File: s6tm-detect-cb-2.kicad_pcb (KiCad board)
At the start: 4 copper layers, 90 x 50 mm, 173 parts, among them J1 Conn_Coaxial, J2 Conn_01x04_Pin, J3 USB_C_Receptacle_USB2.0_14P, J4 Conn_01x04, J5 Conn_01x04, J6 USB_C_Receptacle_USB2.0_14P, J7 Conn_01x04_Pin, J8 SIM_Card_Shielded, J9 Conn_Coaxial, Q1 AO3400A, Q2 MMBT3904, Q3 MMBT3904, Q4 MMBT3904, SW1 SW_Push, SW2 SW_Push, SW3 SW_Push, SW4 SW_Push, U1 W25Q128JVS, U10 TPS6282x, U11 TPS6282x, U12 TPS259472A, U13 TPD3F303DPV, U14 SIM7080G, U15 SN74LV1T125DBV, U16 SN74LV1T125DBV, U17 SN74LV1T125DBV, U18 SN74LV1T125DBV, U19 SN74LV1T125DBV, U2 SN65HVD230, U3 PCF85263ATL, U4 MS5607, U5 ESP32-S3FH4R2, U6 HTU21, U8 VL53L0CXV0DH1, U9 NextPM, Y1 32k768, Y2 48M

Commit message: pcb: route spi flash
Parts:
- moved R8 0.50 mm to (138.5, 85.5)
- moved R9 0.50 mm to (139.5, 85.5)
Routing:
- net /FLASH_CS: track 0.00 -> 19.9 mm
- net /FLASH_IO1: track 0.00 -> 15.8 mm
- net /FLASH_IO0: track 0.00 -> 9.59 mm
- net /FLASH_CLK: track 0.00 -> 5.24 mm
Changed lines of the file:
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@@
 	(footprint "Resistor_SMD:R_0402_1005Metric"
 		(layer "F.Cu")
-		(at 139 85.49 -90)
+		(at 138.5 85.49 -90)
 		(descr "Resistor SMD 0402 (1005 Metric), square (rectangular) end terminal, IPC-7351 nominal, (Body size source: IPC-SM-782 page 72, https://www.pcb-3d.com/wordpress/wp-content/uploads/ipc-sm-782a_amendment_1_and_2.pdf)")
 		(tags "resistor")
@@
 	(footprint "Resistor_SMD:R_0402_1005Metric"
 		(layer "F.Cu")
-		(at 140 85.49 -90)
+		(at 139.5 85.49 -90)
 		(descr "Resistor SMD 0402 (1005 Metric), square (rectangular) end terminal, IPC-7351 nominal, (Body size source: IPC-SM-782 page 72, https://www.pcb-3d.com/wordpress/wp-content/uploads/ipc-sm-782a_amendment_1_and_2.pdf)")
 		(tags "resistor")
@@
 	)
 	(segment
+		(start 146.25 88.25)
+		(end 147.25 87.25)
+		(width 0.2)
+		(layer "F.Cu")
+		(net "/FLASH_CS")
+	)
+	(segment
+		(start 146.9125 77.9125)
+		(end 144.905 77.9125)
+		(width 0.2)
+		(layer "F.Cu")
+		(net "/FLASH_CS")
+	)
+	(segment
+		(start 143.1 88.9)
+		(end 143.75 88.25)
+		(width 0.2)
+		(layer "F.Cu")
+		(net "/FLASH_CS")
+	)
+	(segment
+		(start 143.75 88.25)
+		(end 146.25 88.25)
+		(width 0.2)
+		(layer "F.Cu")
+		(net "/FLASH_CS")
+	)
+	(segment
+		(start 147.25 87.25)
+		(end 147.25 78.25)
+		(width 0.2)
+		(layer "F.Cu")
+		(net "/FLASH_CS")
+	)
+	(segment
+		(start 143.1 90.3)
+		(end 143.1 88.9)
+		(width 0.2)
+		(layer "F.Cu")
+		(net "/FLASH_CS")
+	)
+	(segment
+		(start 144.905 77.9125)
+		(end 144.905 75.895)
+		(width 0.2)
+		(layer "F.Cu")
+		(net "/FLASH_CS")
+	)
+	(segment
+		(start 144.905 75.895)
+		(end 144.76 75.75)
+		(width 0.2)
+		(layer "F.Cu")
+		(net "/FLASH_CS")
+	)
+	(segment
+		(start 147.25 78.25)
+		(end 146.9125 77.9125)
+		(width 0.2)
+		(layer "F.Cu")
+		(net "/FLASH_CS")
+	)
+	(segment
+		(start 141.25 86.5)
+		(end 140.75 86.5)
+		(width 0.2)
+		(layer "F.Cu")
+		(net "/FLASH_IO1")
+	)
+	(segment
+		(start 143.635 80.365)
+		(end 143.635 77.9125)
+		(width 0.2)
+		(layer "F.Cu")
+		(net "/FLASH_IO1")
+	)
+	(segment
+		(start 140.25 82)
+		(end 141 81.25)
+		(width 0.2)
+		(layer "F.Cu")
+		(net "/FLASH_IO1")
+	)
+	(segment
+		(start 141 81.25)
+		(end 142.75 81.25)
+		(width 0.2)
+		(layer "F.Cu")
+		(net "/FLASH_IO1")
+	)
+	(segment
+		(start 142.75 81.25)
+		(end 143.635 80.365)
+		(width 0.2)
+		(layer "F.Cu")
+		(net "/FLASH_IO1")
+	)
+	(segment
+		(start 140.75 86.5)
+		(end 140.25 86)
+		(width 0.2)
+		(layer "F.Cu")
+		(net "/FLASH_IO1")
+	)
+	(segment
+		(start 141.9 90.3)
+		(end 141.9 87.15)
+		(width 0.2)
+		(layer "F.Cu")
+		(net "/FLASH_IO1")
+	)
+	(segment
+		(start 140.25 86)
+		(end 140.25 82)
+		(width 0.2)
+		(layer "F.Cu")
+		(net "/FLASH_IO1")
+	)
+	(segment
+		(start 141.9 87.15)
+		(end 141.25 86.5)
+		(width 0.2)
+		(layer "F.Cu")
+		(net "/FLASH_IO1")
+	)
+	(segment
+		(start 143 84)
+		(end 142.75 83.75)
+		(width 0.2)
+		(layer "F.Cu")
+		(net "/FLASH_IO0")
+	)
+	(segment
+		(start 141.405 83.75)
+		(end 141.095 84.06)
+		(width 0.2)
+		(layer "F.Cu")
+		(net "/FLASH_IO0")
+	)
+	(segment
+		(start 142.75 83.75)
+		(end 141.405 83.75)
+		(width 0.2)
+		(layer "F.Cu")
+		(net "/FLASH_IO0")
+	)
+	(segment
+		(start 141.095 84.06)
+		(end 141.095 85.0875)
+		(width 0.2)
+		(layer "F.Cu")
+		(net "/FLASH_IO0")
+	)
+	(segment
+		(start 142.7 90.3)
+		(end 142.7 86.3)
+		(width 0.2)
+		(layer "F.Cu")
+		(net "/FLASH_IO0")
+	)
+	(segment
+		(start 142.7 86.3)
+		(end 143 86)
+		(width 0.2)
+		(layer "F.Cu")
+		(net "/FLASH_IO0")
+	)
+	(segment
+		(start 143 86)
+		(end 143 84)
+		(width 0.2)
+		(layer "F.Cu")
+		(net "/FLASH_IO0")
+	)
+	(segment
+		(start 142.3 85.1525)
+		(end 142.365 85.0875)
+		(width 0.2)
+		(layer "F.Cu")
+		(net "/FLASH_CLK")
+	)
+	(segment
+		(start 142.3 90.3)
+		(end 142.3 85.1525)
+		(width 0.2)
+		(layer "F.Cu")
+		(net "/FLASH_CLK")
+	)
+	(segment

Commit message: pcb: route can
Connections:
- U5 pad 13: /CAN_RX -> /CAN_TX
- U5 pad 14: /CAN_TX -> /CAN_RX
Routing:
- net CANL: track 0.00 -> 40.5 mm
- net /CAN_RX: track 0.00 -> 35.8 mm
- net /CAN_TX: track 0.00 -> 31.6 mm
- net CANH: track 0.00 -> 30.0 mm
- net Net-(JP1-B): track 0.00 -> 2.89 mm
- net GND: vias 188 -> 192

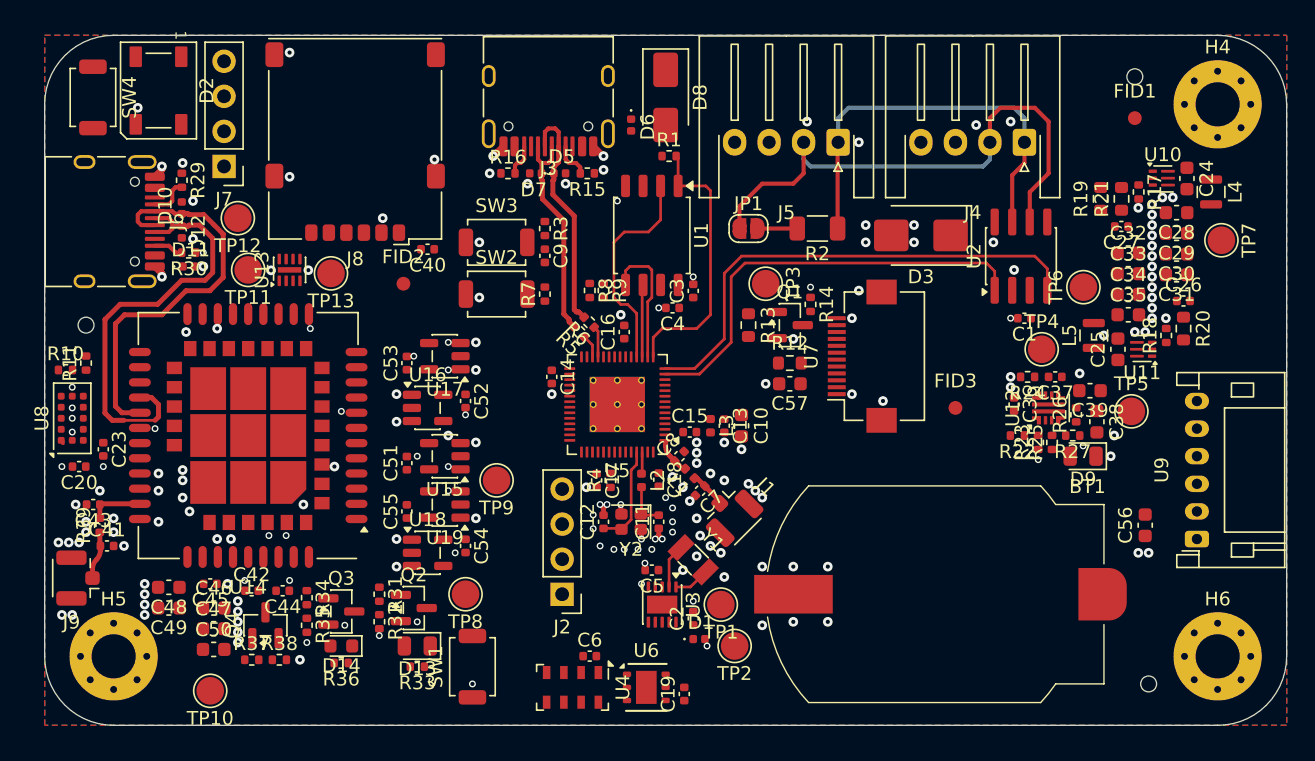
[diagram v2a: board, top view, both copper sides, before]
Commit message: pcb: route uarts
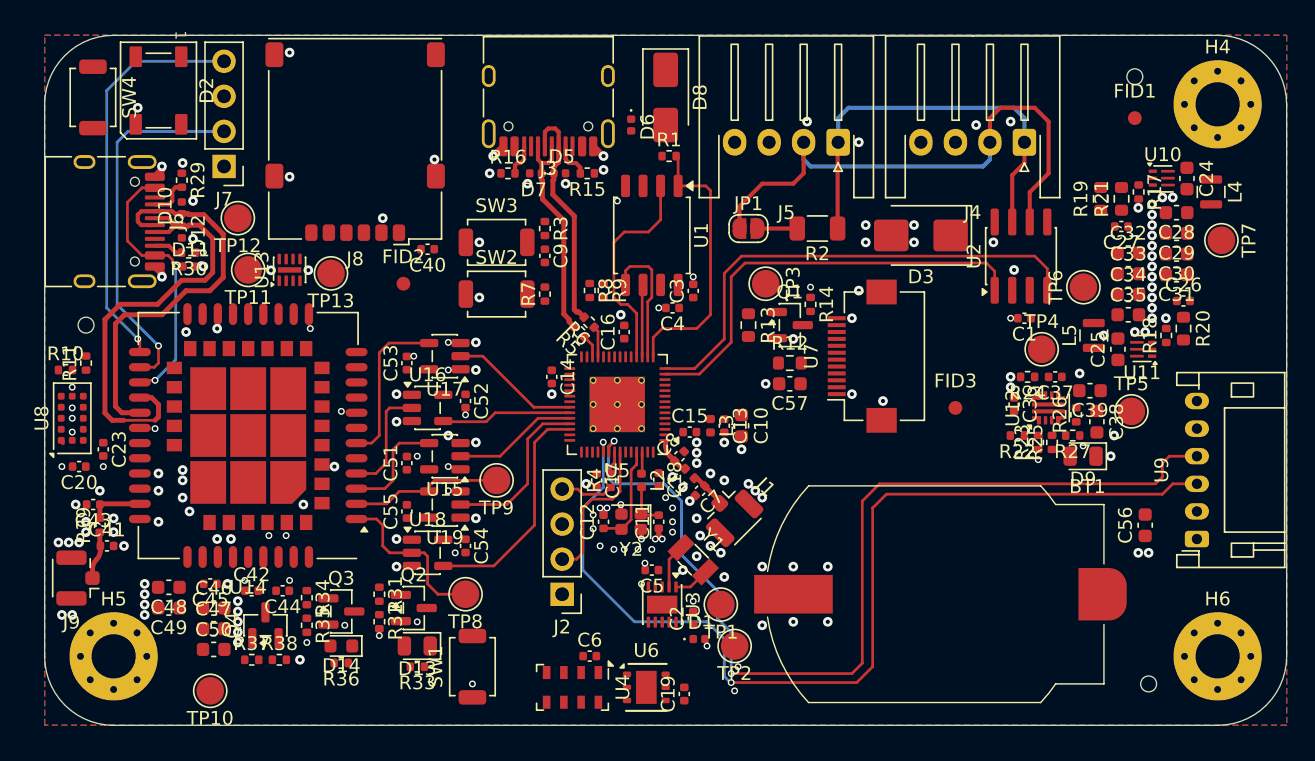
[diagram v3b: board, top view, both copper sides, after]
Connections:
- U5 pad 47: /PM_RX -> /PM_TX
- U5 pad 48: /PM_TX -> /PM_RX
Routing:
- net /PM_TX: track 0.00 -> 72.8 mm, vias 0 -> 2
- net /PM_RX: track 0.00 -> 71.6 mm, vias 0 -> 2
- net /Cellular/UART2_TXD: track 0.00 -> 29.3 mm, vias 0 -> 1
- net /Cellular/UART2_RXD: track 0.00 -> 26.8 mm, vias 0 -> 1
- net /Cellular/VBUS: track 0.00 -> 20.2 mm, vias 0 -> 2
- net SIM_TXD: track 0.00 -> 16.8 mm
- net SIM_RXD: track 0.00 -> 12.2 mm
- net /Cellular/UART1_TXD: track 0.00 -> 12.2 mm
- net /Cellular/UART1_DTR: track 0.00 -> 11.8 mm
- net /Cellular/UART1_RXD: track 0.00 -> 11.1 mm
- net /U0RXD: track 0.00 -> 11.0 mm
- net SIM_CTS: track 0.00 -> 9.45 mm
- net SIM_DTR: track 0.00 -> 9.45 mm
- net SIM_RTS: track 0.00 -> 9.05 mm
- net /Cellular/UART1_CTS: track 0.00 -> 8.18 mm
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
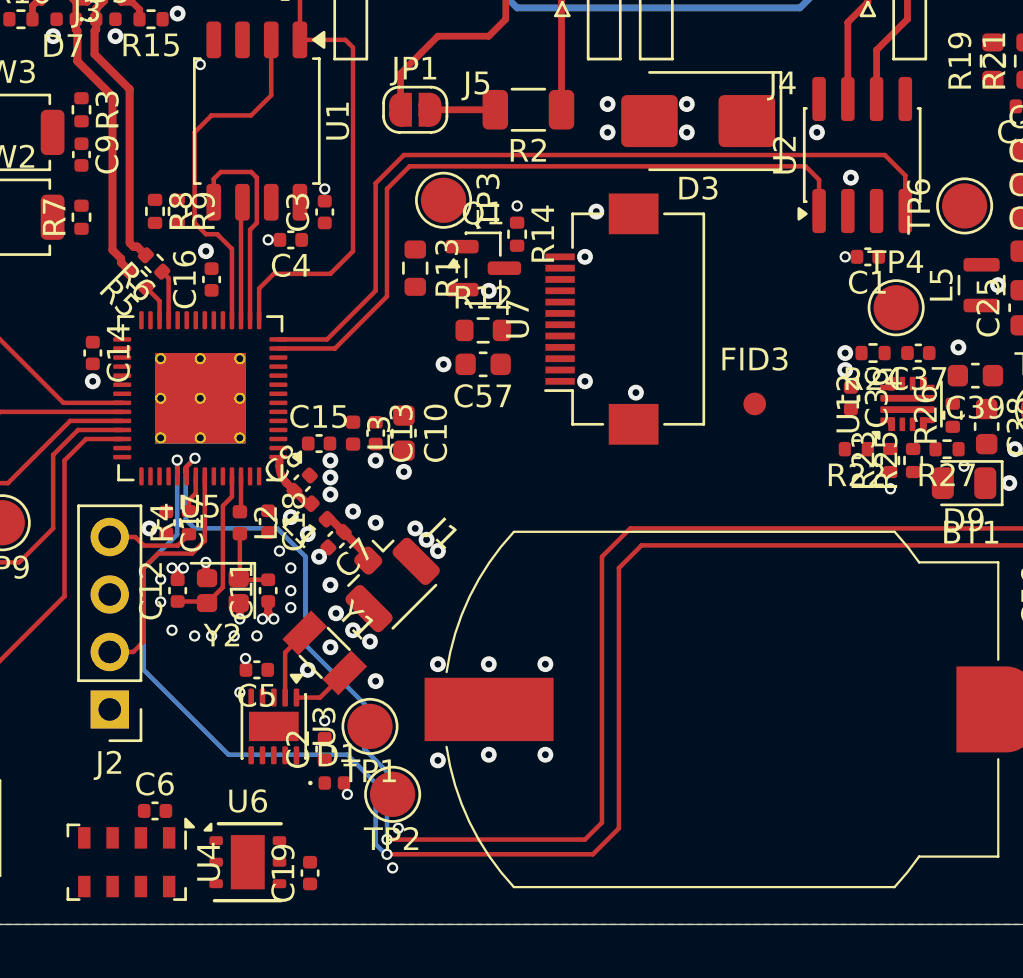
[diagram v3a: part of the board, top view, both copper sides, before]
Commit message: pcb: route tft spi display
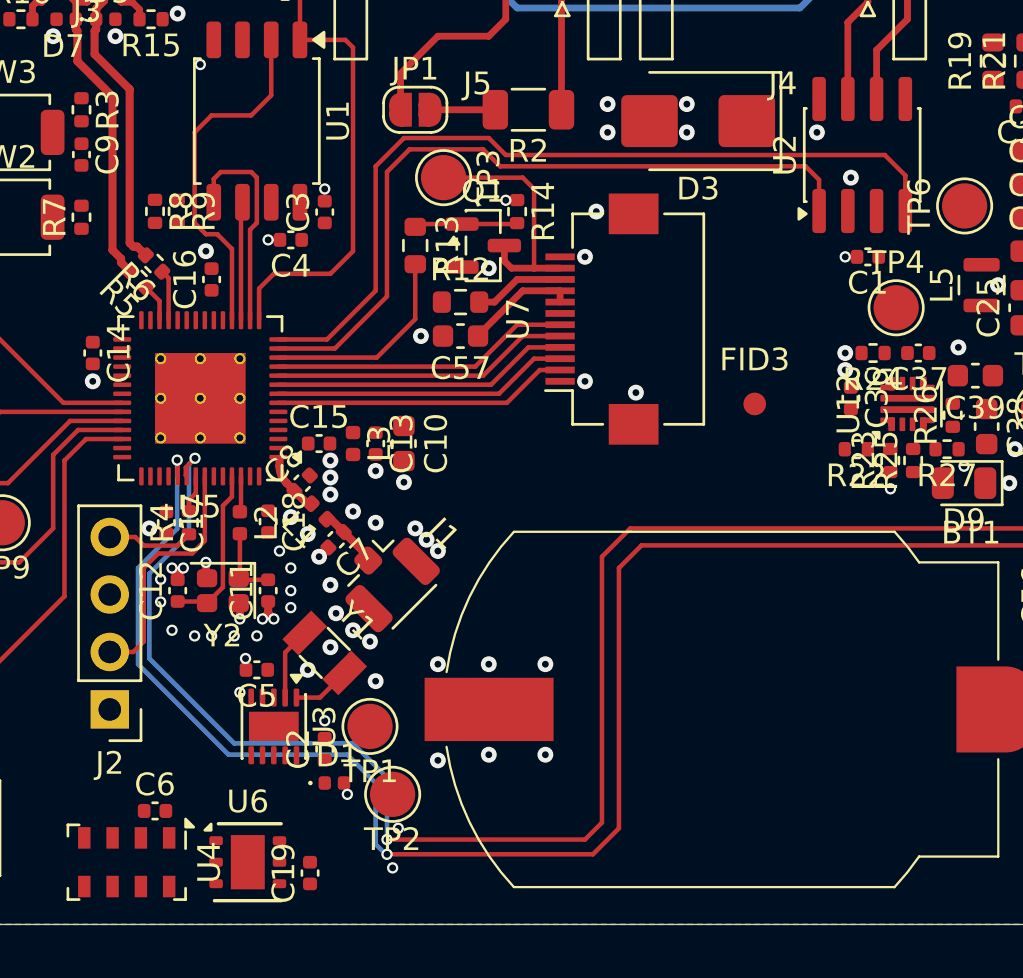
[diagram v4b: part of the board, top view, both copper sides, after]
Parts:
- moved C57 1.60 mm to (152.0, 91.0)
- moved R12 1.60 mm to (152.0, 89.5)
- moved Q1 1.00 mm to (153.0, 87.0)
- moved R13 1.00 mm to (150.0, 87.0)
- moved R14 1.00 mm to (154.5, 85.5)
- moved TP3 1.00 mm to (151.2, 84.0)
- moved C10 0.46 mm to (149.5, 95.8)
- moved C13 0.46 mm to (148.2, 95.8)
- moved L3 0.46 mm to (147.2, 95.8)
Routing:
- net /RESET: track 0.00 -> 13.2 mm
- net /MOSI: track 0.00 -> 13.2 mm
- net /SCLK: track 0.00 -> 13.1 mm
- net /DC: track 0.00 -> 13.1 mm
- net /TFT_CS: track 0.00 -> 13.1 mm
- net Net-(Q1-D): track 0.00 -> 11.0 mm
- net /B_LED: track 0.00 -> 9.18 mm
- net +3V3: track 0.00 -> 4.97 mm
- net Net-(Q1-G): track 0.00 -> 4.57 mm
- net Net-(U7-LED+): track 0.00 -> 3.99 mm
- net /PM_RX: track 71.6 -> 73.8 mm
- net /CAN_TX: track 31.6 -> 32.7 mm
- net /CAN_RX: track 35.8 -> 36.9 mm

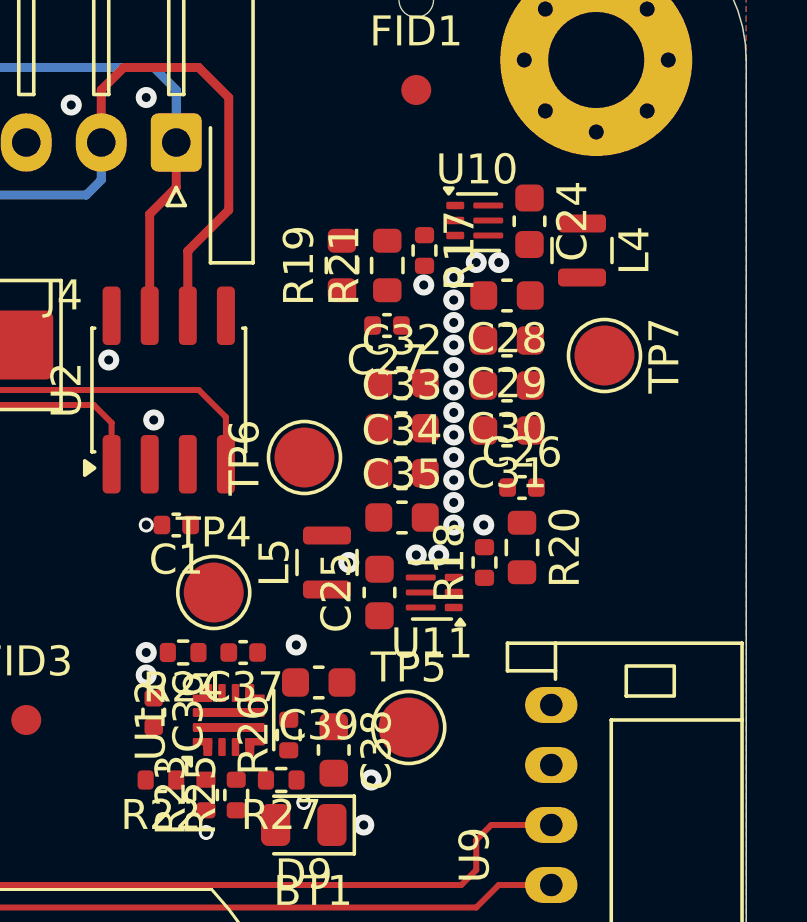
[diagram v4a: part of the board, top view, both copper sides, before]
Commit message: pcb: route smpss
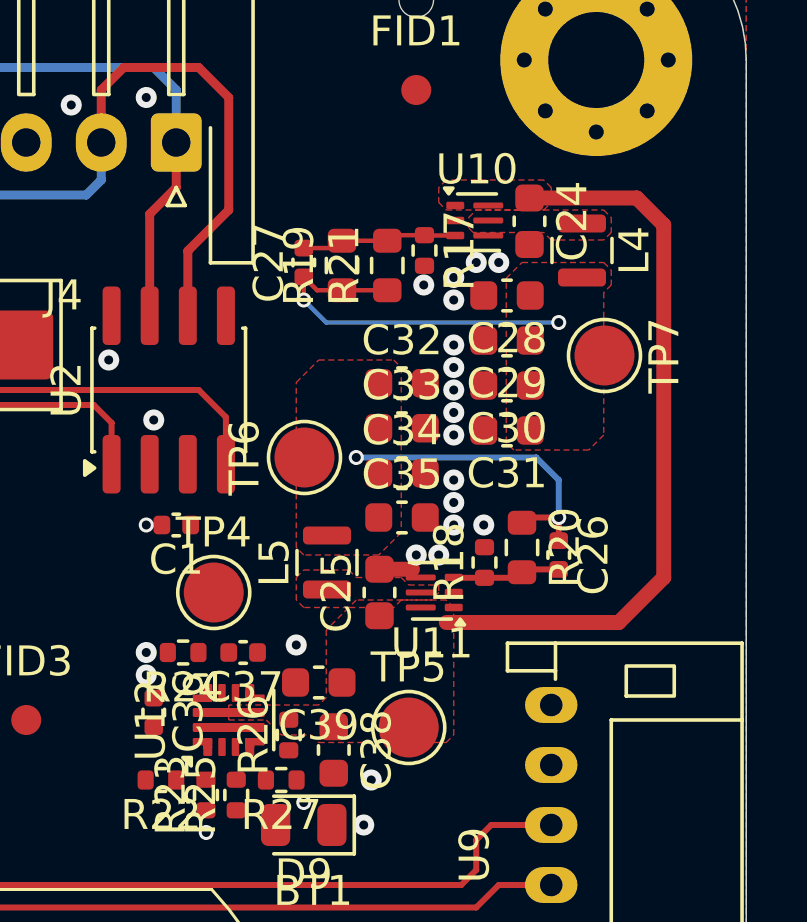
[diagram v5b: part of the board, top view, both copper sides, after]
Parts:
- moved C27 3.48 mm to (174.2, 78.8), turned to 90 degrees
- moved C26 2.56 mm to (182.8, 88.5), turned to -90 degrees
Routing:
- net +5V: track 0.00 -> 24.5 mm
- net +3V8: track 0.00 -> 12.5 mm, vias 0 -> 2
- net +3V3: track 4.97 -> 15.3 mm, vias 0 -> 2
- net Net-(U10-FB): track 0.00 -> 5.23 mm
- net Net-(U11-FB): track 0.00 -> 3.62 mm
- net GND: track 7.66 -> 8.76 mm, vias 194 -> 191
- added copper zone on F.Cu, net +3V3
- added copper zone on F.Cu, net +3V8
- added copper zone on F.Cu, net +5V
- added copper zone on F.Cu, net Net-(U10-SW)
- added copper zone on F.Cu, net Net-(U11-SW)

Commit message: pcb: route sim
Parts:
- moved C40 0.71 mm to (126.2, 83.0)
- moved U13 0.21 mm to (116.8, 84.2)
- moved TP13 0.19 mm to (119.8, 84.4)
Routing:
- net Net-(J8-VCC): track 0.00 -> 26.0 mm, vias 0 -> 2
- net Net-(J8-CLK): track 0.00 -> 12.2 mm
- net Net-(U13-DATA2_OUT): track 0.00 -> 11.6 mm
- net Net-(J8-RST): track 0.00 -> 6.93 mm
- net Net-(U13-CLK_OUT): track 0.00 -> 5.72 mm
- net Net-(U13-DATA1_OUT): track 0.00 -> 4.88 mm
- net Net-(J8-I/O): track 0.00 -> 3.97 mm
